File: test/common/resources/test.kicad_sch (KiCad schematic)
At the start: 4 parts, among them U1 4011, U2 LM4990ITL

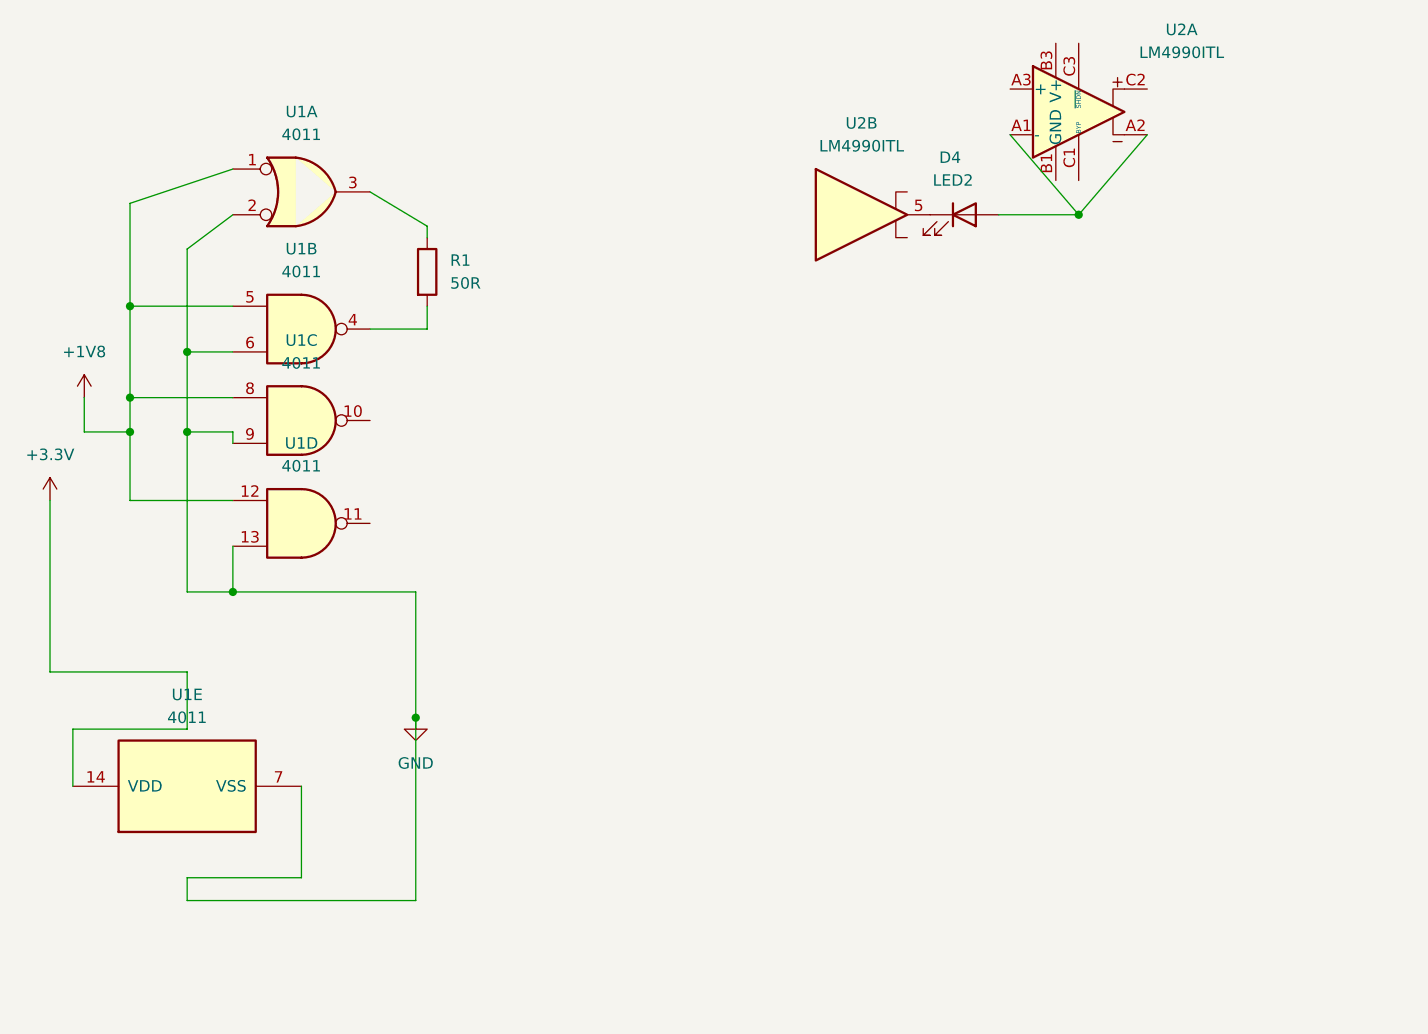
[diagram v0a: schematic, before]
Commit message: schematic importer: import labels
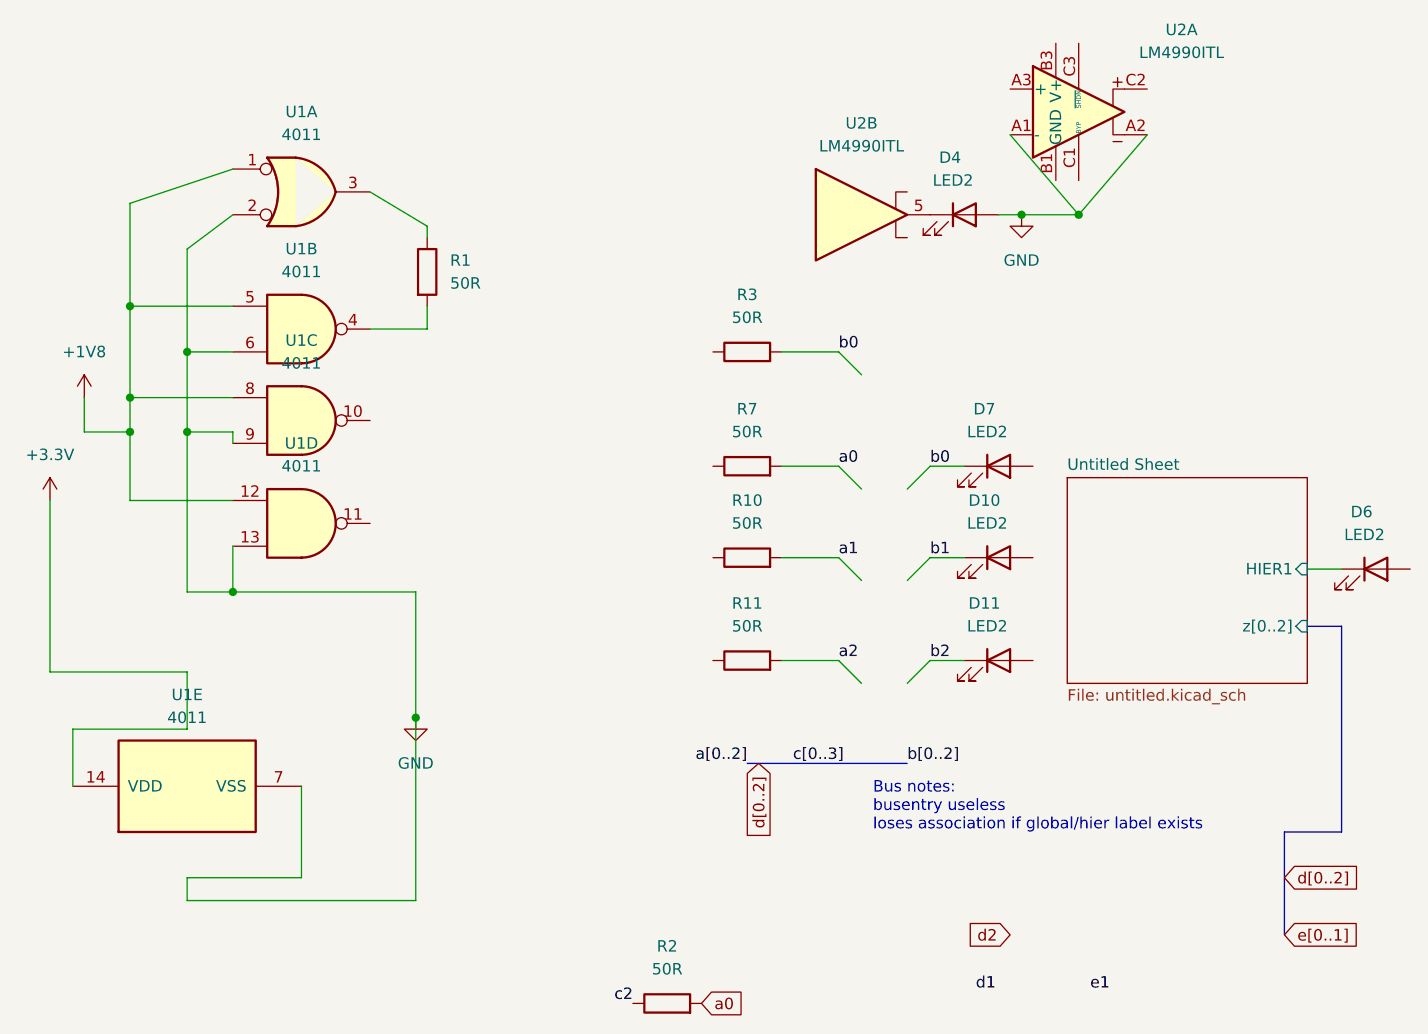
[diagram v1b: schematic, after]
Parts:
- added D10, D11, D6, D7: LED2, Resistor_SMD:R_0603_1608Metric, symbol Device:LED
- added R10, R11, R2, R3, R7: 50R, Resistor_SMD:R_0805_2012Metric, symbol Device:R
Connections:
- net GND: now also D4.2 (A), U2.A1 (-), U2.A2
- new net Untitled Sheet/HIER1: D6.1 (K)
- new net a0: R2.2, R7.2
- new net a1: R10.2
- new net a2: R11.2
- new net b0: D7.1 (K), R3.2
- new net b1: D10.1 (K)
- new net b2: D11.1 (K)
- new net c2: R2.1
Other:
- added sheet Untitled Sheet (untitled.kicad_sch)
- note added: "Bus notes: busentry useless loses association if global/hier label exists"
